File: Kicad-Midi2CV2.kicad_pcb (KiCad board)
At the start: 2 copper layers, 100 x 100 mm, 115 parts, among them IC101 MCP4725module, IC102 MCP4725module, J101 Doepfer connector, J102 Vin 7-12v, J103 MIDI OUT, J104 Power Conn, J105 CV7 in, J106 Gate1, J107 MIDI IN, J108 CV6 in, J109 Gate2, J110 CV3 in, J111 Gate3, J112 CV1, J113 Gate4, J114 CV2, J115 ControlConn, J116 ControlConn, J117 I2C_Conn, J118 I2C_Conn, Q101 MMBT2222A, Q102 MMBT2222A, SW101 Rotary_Encoder_Switch, U101 TL072, U102 TL072, U103 EL814

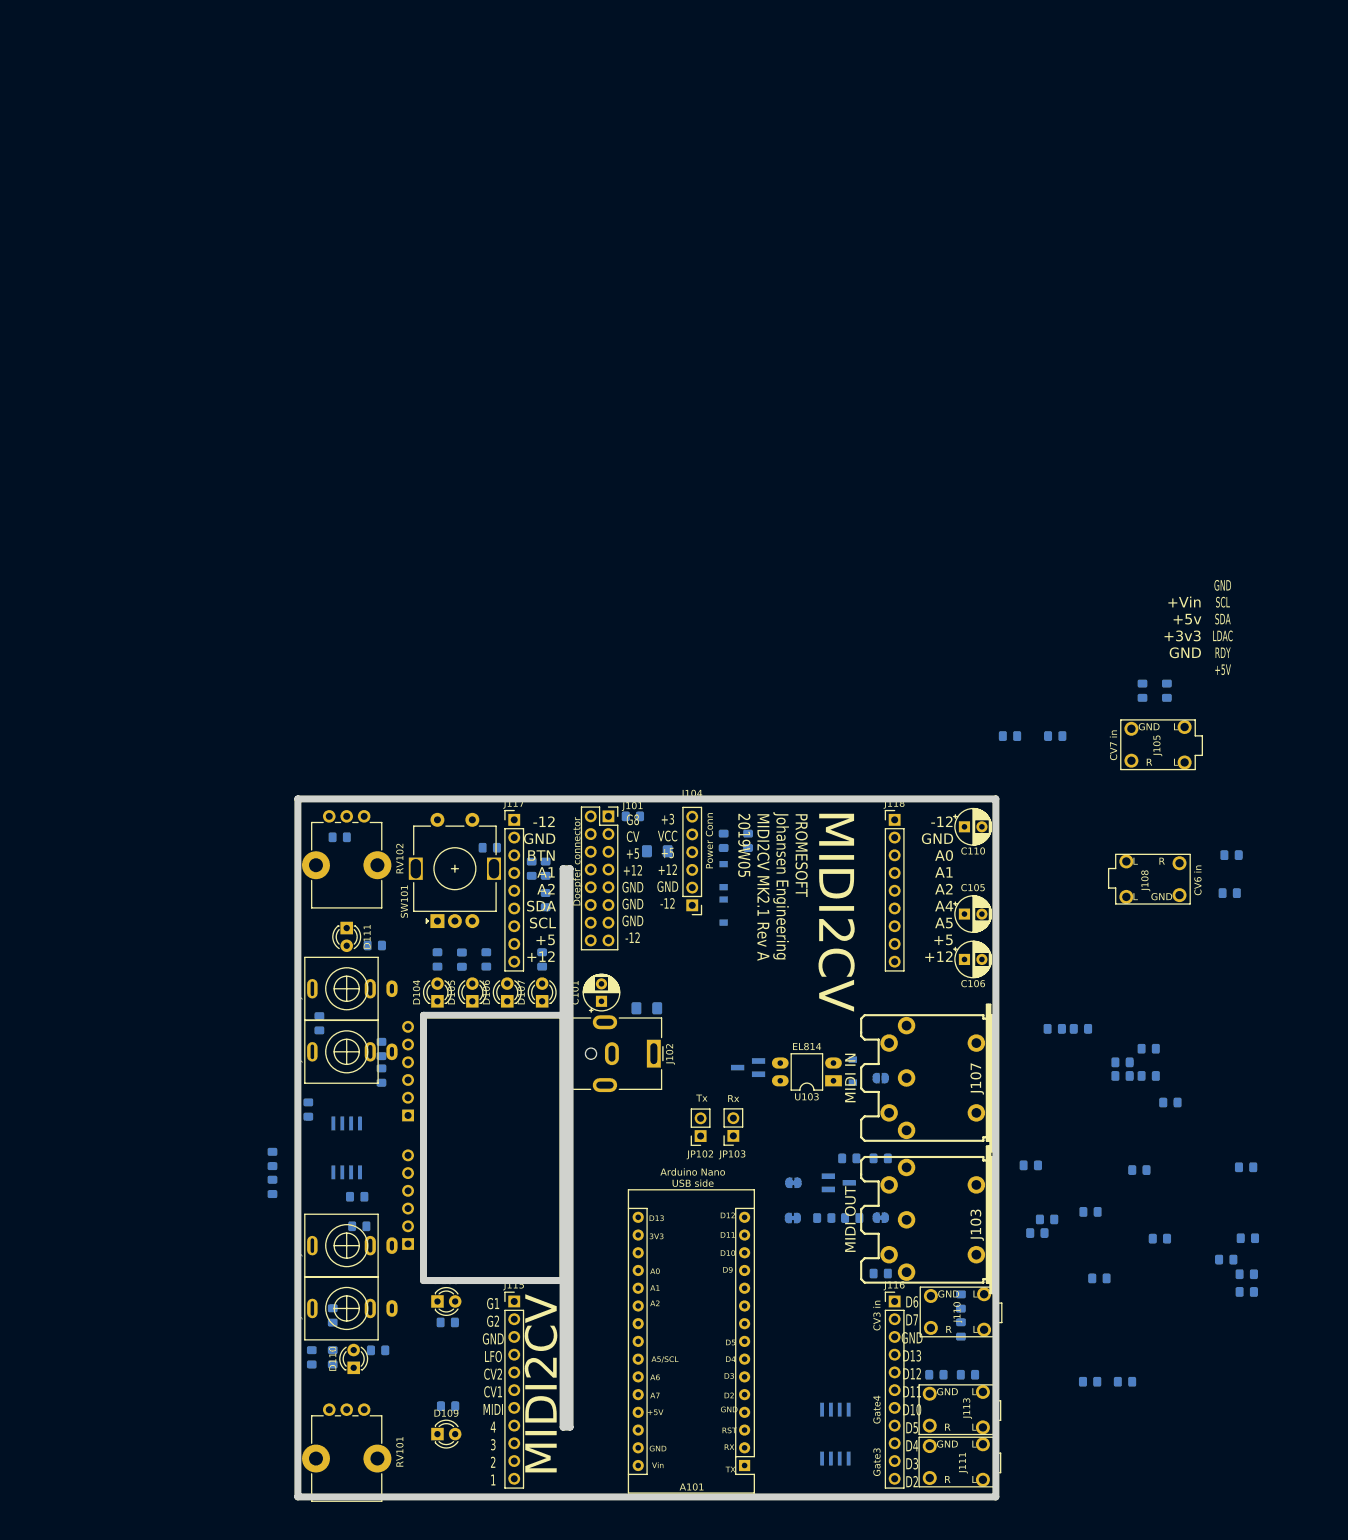
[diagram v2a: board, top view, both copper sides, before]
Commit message: Component replacement
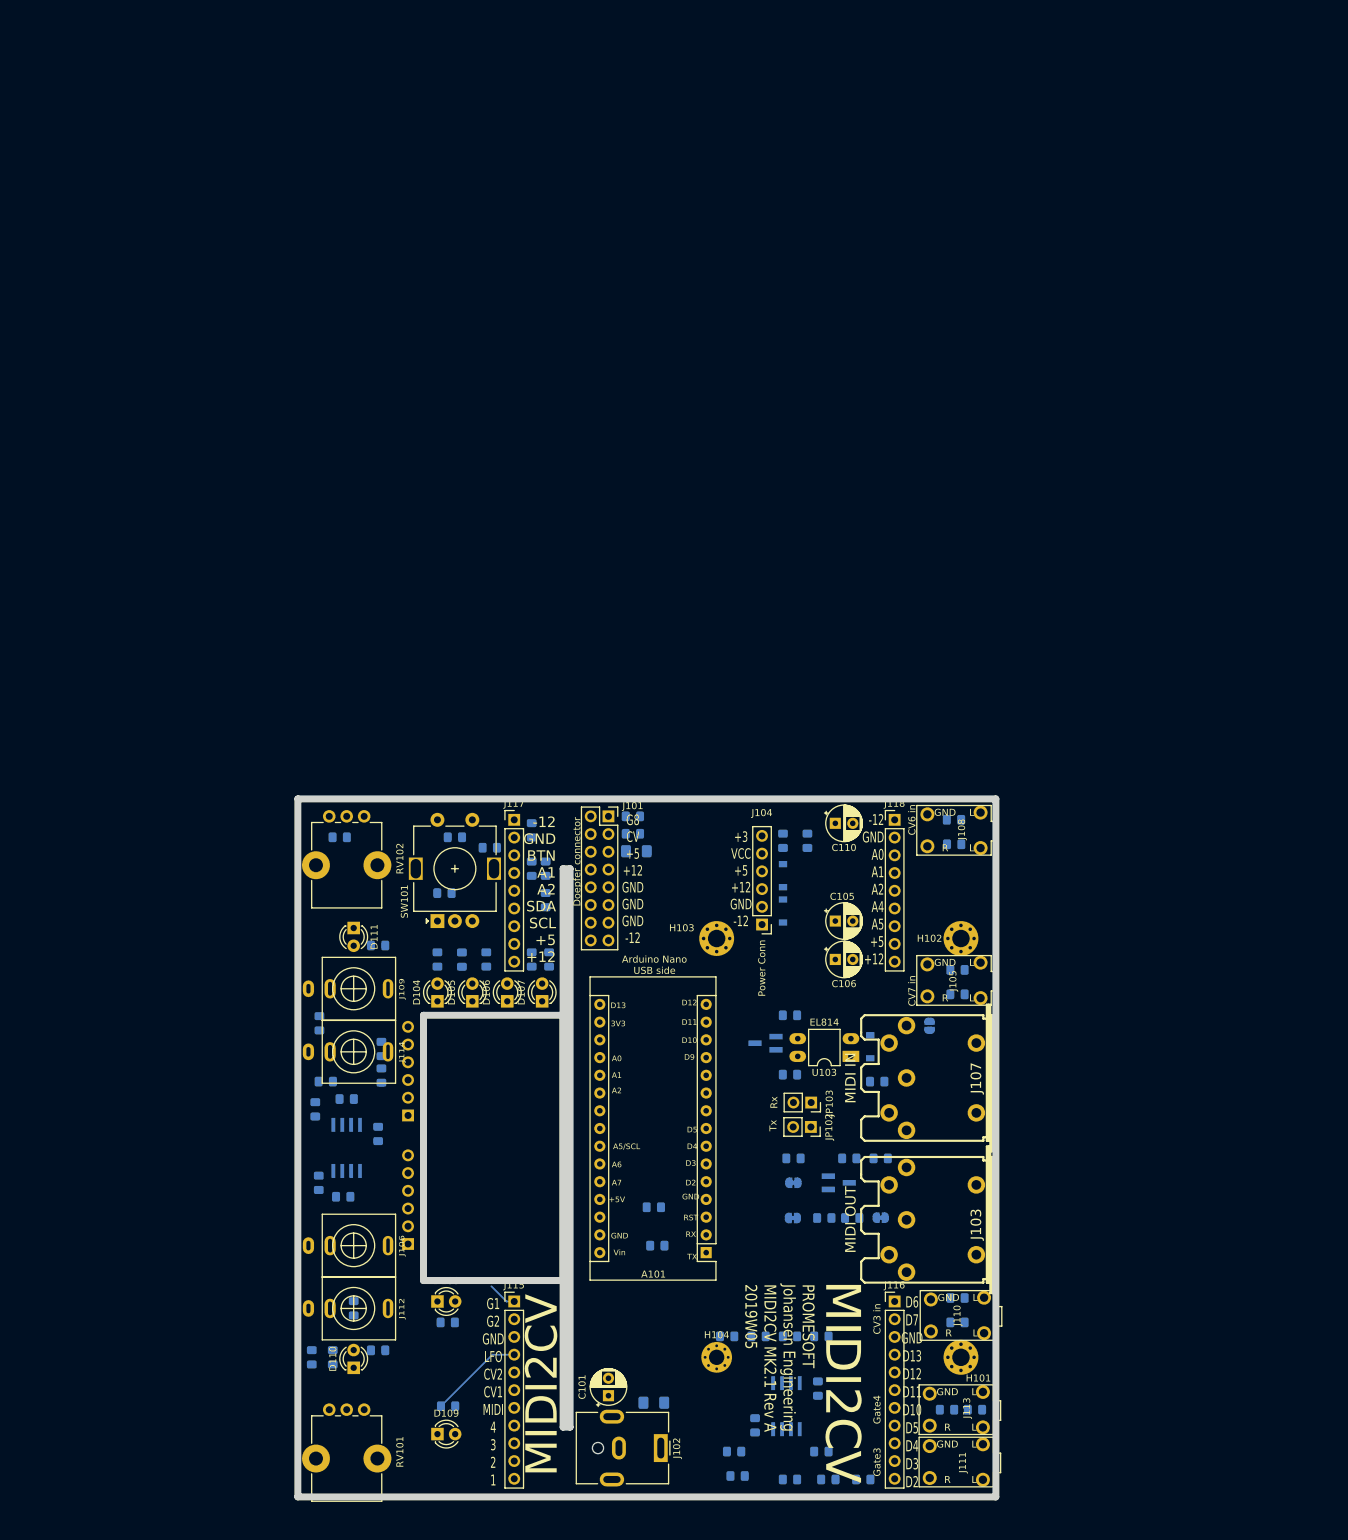
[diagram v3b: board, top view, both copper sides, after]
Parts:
- added H101: 2,5mm, MountingHole:MountingHole_2.5mm_Pad_Via, F.Cu at (195.0, 130.0)
- added H102: 2,5mm, MountingHole:MountingHole_2.5mm_Pad_Via, F.Cu at (195.0, 70.0)
- added H103: 2,2mm, MountingHole:MountingHole_2.5mm_Pad_Via, F.Cu at (160.0, 70.0)
- added H104: 2,2mm, MountingHole:MountingHole_2.2mm_M2_Pad_Via, F.Cu at (160.0, 130.0)
- C114: value 47n -> 11n
- C115: value 47n -> 22n
- C117, C118: value 100n -> 33n
- C119, C120: value 100n -> 44n
- R104, R105: value 10k -> 11k
- R108: value 100R -> 110R
- R113, R114: value 10k -> 22k
- R118: value 100R -> 220R
- R123, R124, R128, R129: value 10k -> 33k
- R135, R136, R138, R139: value 10k -> 44k
- moved C115 135.3 mm to (104.0, 90.5)
- moved R123 111.3 mm to (162.5, 143.5), turned to 180 degrees
- moved R144 103.3 mm to (121.0, 63.5)
- moved C121 100.9 mm to (122.5, 55.5)
- moved C116 84.5 mm to (151.5, 114.0)
- moved C109 81.5 mm to (133.5, 73.0), turned to 90 degrees
- moved R114 80.5 mm to (107.0, 93.0)
- moved R102 79.2 mm to (148.0, 55.0), turned to 180 degrees
- moved C118 78.5 mm to (163.0, 147.0)
- moved R127 73.2 mm to (194.0, 53.0)
- moved R138 71.8 mm to (161.5, 127.0)
- moved C117 70.0 mm to (170.5, 147.5)
- moved C113 69.8 mm to (133.5, 54.5), turned to 270 degrees
- moved C103 64.6 mm to (151.0, 108.5), turned to 180 degrees
- moved C119 64.1 mm to (166.0, 127.0)
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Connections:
- J106 pad S: Net-(J106-PadS) -> GND
- J109 pad S: Net-(J106-PadS) -> GND
- J111 pad S: Net-(J106-PadS) -> GND
- J113 pad S: Net-(J106-PadS) -> GND
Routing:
- net LED_LFO: track 0.00 -> 13.6 mm
- net Gate1: track 0.00 -> 4.18 mm
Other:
- board text removed: "+Vin +5v +3v3 GND"
- board text removed: "GND SCL SDA LDAC RDY +5V"

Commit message: Routing....
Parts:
- moved R141 10.0 mm to (121.5, 147.0)
- moved C115 7.63 mm to (110.5, 86.5), turned to 90 degrees
- moved C104 7.42 mm to (110.5, 82.5)
- moved R144 6.40 mm to (117.0, 68.5), turned to 90 degrees
- moved C121 5.70 mm to (128.0, 57.0), turned to 180 degrees
- moved R143 4.95 mm to (108.0, 74.5), turned to 90 degrees
- moved IC101 4.24 mm to (115.5, 118.0)
- moved R146 4.03 mm to (128.0, 53.0)
- moved C109 3.64 mm to (132.5, 76.5)
- moved R106 3.48 mm to (113.0, 82.5)
- moved R118 1.80 mm to (107.0, 57.0), turned to 90 degrees
- moved R107 1.09 mm to (113.0, 90.0)
- moved IC102 0.90 mm to (115.5, 94.5)
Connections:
- J115 pad 1: Gate1 -> LED4
- J115 pad 10: LED2 -> LED-CV1
- J115 pad 11: LED1 -> LED_LFO
- J115 pad 2: Gate2 -> LED3
- J115 pad 3: Net-(J115-Pad3) -> LED2
- J115 pad 4: LED_LFO -> LED1
- J115 pad 5: LED-CV2 -> Gate2
- J115 pad 6: LED-CV1 -> Gate1
- J115 pad 7: LED-MIDI -> GND
- J115 pad 8: LED4 -> LED-CV2
- J115 pad 9: LED3 -> LED-MIDI
- J116 pad 1: Gate1 -> LED4
- J116 pad 10: LED2 -> LED-CV1
- J116 pad 11: LED1 -> LED_LFO
- J116 pad 2: Gate2 -> LED3
- J116 pad 3: Net-(J115-Pad3) -> LED2
- J116 pad 4: LED_LFO -> LED1
- J116 pad 5: LED-CV2 -> Gate2
- J116 pad 6: LED-CV1 -> Gate1
- J116 pad 7: LED-MIDI -> GND
- J116 pad 8: LED4 -> LED-CV2
- J116 pad 9: LED3 -> LED-MIDI
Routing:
- net SDA: track 0.00 -> 64.0 mm
- net SCL: track 0.00 -> 61.8 mm
- net Net-(R118-Pad2): track 0.00 -> 52.2 mm
- net +5V: track 0.00 -> 47.9 mm, vias 0 -> 3
- net Net-(R108-Pad2): track 0.00 -> 45.7 mm
- net Net-(R114-Pad1): track 0.00 -> 42.7 mm, vias 0 -> 2
- net CV2Gain: track 0.00 -> 34.1 mm
- net GND: track 0.00 -> 32.5 mm
- net Net-(R104-Pad1): track 0.00 -> 28.0 mm
- net Gate1: track 4.18 -> 32.1 mm
- net LED-CV1: track 0.00 -> 27.7 mm
- net LED-MIDI: track 0.00 -> 23.3 mm
- net A1: track 0.00 -> 20.3 mm
- net CV1: track 0.00 -> 18.1 mm
- net A2: track 0.00 -> 14.9 mm
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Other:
- board text added: "4 3 2 1 G2 G1 GND CV2 MIDI CV1 LFO"
- board text added: "D5 D4 D3 D2 D7 D6 GND D12 D10 D11 D13"
- board text removed: "D6 D7 GND D13 D12 D11 D10 D5 D4 D3 D2"
- board text removed: "G1 G2 GND LFO CV2 CV1 MIDI 4 3 2 1"

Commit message: front routed....
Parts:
- moved C114 0.50 mm to (108.5, 123.0)
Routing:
- net LED2: track 0.00 -> 138.5 mm, vias 0 -> 4
- net LED1: track 0.00 -> 138.4 mm, vias 0 -> 9
- net LED4: track 0.00 -> 104.4 mm, vias 0 -> 7
- net LED3: track 0.00 -> 95.0 mm, vias 0 -> 7
- net Gate2: track 0.00 -> 73.4 mm, vias 0 -> 6
- net -12V: track 5.41 -> 77.8 mm, vias 0 -> 4
- net +12V: track 5.15 -> 73.9 mm, vias 0 -> 8
- net +5V: track 47.9 -> 71.7 mm, vias 3 -> 4
- net GND: track 32.5 -> 54.0 mm, vias 0 -> 4
- net CV1Gain: track 8.27 -> 13.1 mm, vias 0 -> 1
- net CV2Gain: track 34.1 -> 36.1 mm
- net Gate1: track 32.1 -> 33.5 mm
- net CV1: track 18.1 -> 18.9 mm
- net Net-(R118-Pad2): track 52.2 -> 52.8 mm

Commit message: Initial PCB finished - no DRC
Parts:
- added R147: 133R, Resistor_SMD:R_0805_2012Metric_Pad1.15x1.40mm_HandSolder, B.Cu at (177.0, 141.0)
- added R148: 144R, Resistor_SMD:R_0805_2012Metric_Pad1.15x1.40mm_HandSolder, B.Cu at (173.0, 128.0)
- JP104: value GND MIDI OUT -> GND MIDI IN
- moved C116 36.9 mm to (175.0, 85.5), turned to 270 degrees
- moved R135 26.6 mm to (169.0, 126.0)
- moved R136 26.6 mm to (173.0, 126.0)
- moved R128 12.3 mm to (169.0, 145.0), turned to 180 degrees
- moved R111 9.53 mm to (179.0, 105.0)
- moved C119 7.62 mm to (173.0, 124.0), turned to 180 degrees
- moved C118 7.21 mm to (169.0, 143.0), turned to 180 degrees
- moved C105 7.00 mm to (177.0, 60.5)
- moved R123 6.96 mm to (169.0, 141.0)
- moved C120 6.71 mm to (169.0, 124.0), turned to 180 degrees
- moved R139 6.18 mm to (169.0, 121.0)
- moved C117 5.15 mm to (173.0, 143.0)
- moved R115 5.00 mm to (171.0, 110.0), turned to 0 degrees
- moved C103 4.61 mm to (146.5, 107.5)
- moved R138 4.61 mm to (165.0, 124.0), turned to 180 degrees
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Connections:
- U102 pad 1: Gate3Gain -> Net-(R147-Pad2)
- U102 pad 7: Gate4Gain -> Net-(R148-Pad2)
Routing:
- net +5V: track 71.7 -> 251.3 mm, vias 4 -> 6
- net LED-CV2: track 0.00 -> 176.5 mm, vias 0 -> 6
- net -12V: track 77.8 -> 245.5 mm, vias 4 -> 12
- net +12V: track 73.9 -> 217.2 mm, vias 8 -> 15
- net GND: track 54.0 -> 194.2 mm, vias 4 -> 14
- net A7: track 0.00 -> 131.8 mm, vias 0 -> 1
- net A3: track 0.00 -> 115.0 mm, vias 0 -> 5
- net A6: track 0.00 -> 113.3 mm, vias 0 -> 1
- net LED_LFO: track 12.1 -> 121.7 mm
- net VCC: track 0.00 -> 103.4 mm, vias 0 -> 3
- net LED-CV1: track 27.7 -> 119.4 mm
- net LED-MIDI: track 23.3 -> 104.9 mm
- net Gate3: track 0.00 -> 62.2 mm, vias 0 -> 2
- net SCL: track 61.8 -> 123.5 mm
- net Gate1: track 33.5 -> 93.0 mm
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- added copper zone on F.Cu, net GND

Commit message: GND plane
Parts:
- moved R137 0.60 mm to (135.4, 73.0)
- moved C114 0.50 mm to (109.0, 123.0)
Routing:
- net A3: track 115.0 -> 125.5 mm
- net +12V: track 217.2 -> 224.6 mm
- net GND: track 194.2 -> 200.8 mm, vias 14 -> 15
- net LED-CV2: track 176.5 -> 182.1 mm, vias 6 -> 8
- net LED2: track 175.8 -> 179.9 mm, vias 4 -> 10
- net CV1Gain: track 13.1 -> 16.9 mm
- net Net-(R114-Pad1): track 42.7 -> 46.3 mm
- net -12V: track 245.5 -> 247.5 mm, vias 12 -> 10
- net Net-(J105-PadT): track 11.5 -> 10.0 mm
- net Net-(R104-Pad1): track 28.2 -> 29.6 mm
- net Gate4Gain: track 42.1 -> 43.3 mm
- net LED1: track 175.7 -> 176.8 mm, vias 9 -> 11
- net Gate3Gain: track 36.6 -> 35.6 mm
- net /Q1Emitter: track 20.4 -> 20.9 mm
- net Gate2: track 128.8 -> 128.3 mm
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
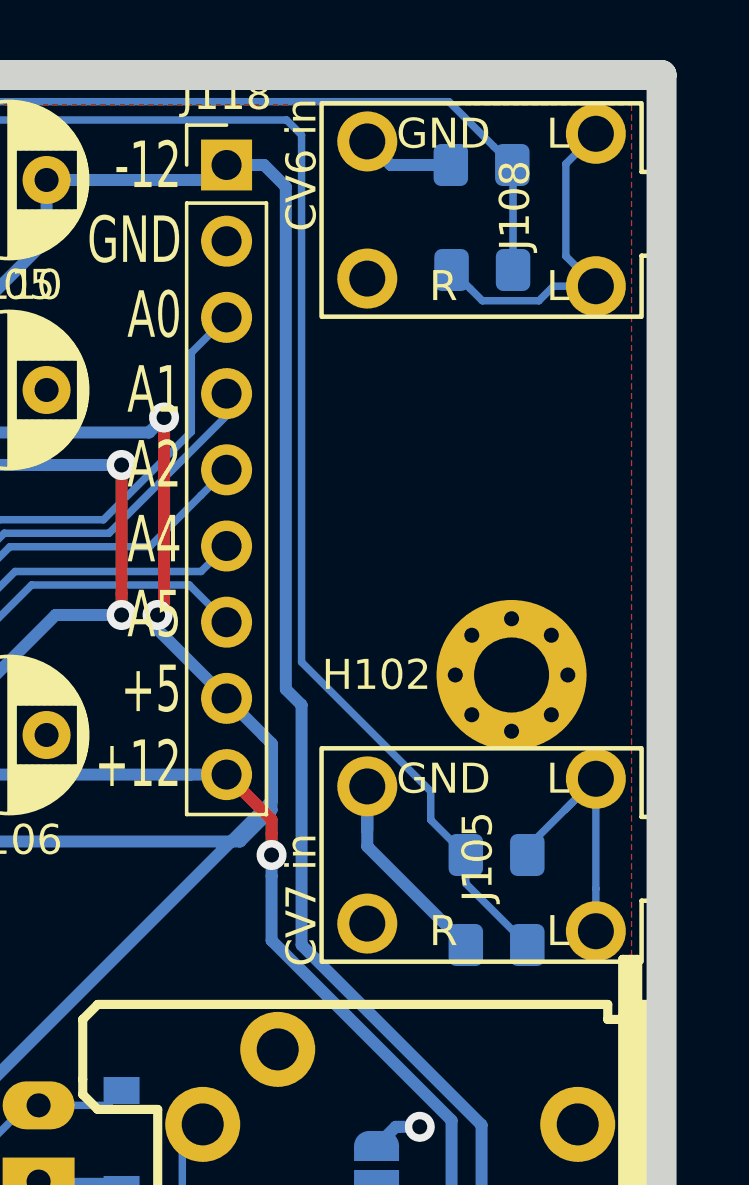
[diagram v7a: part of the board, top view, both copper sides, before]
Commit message: Component text on PCB
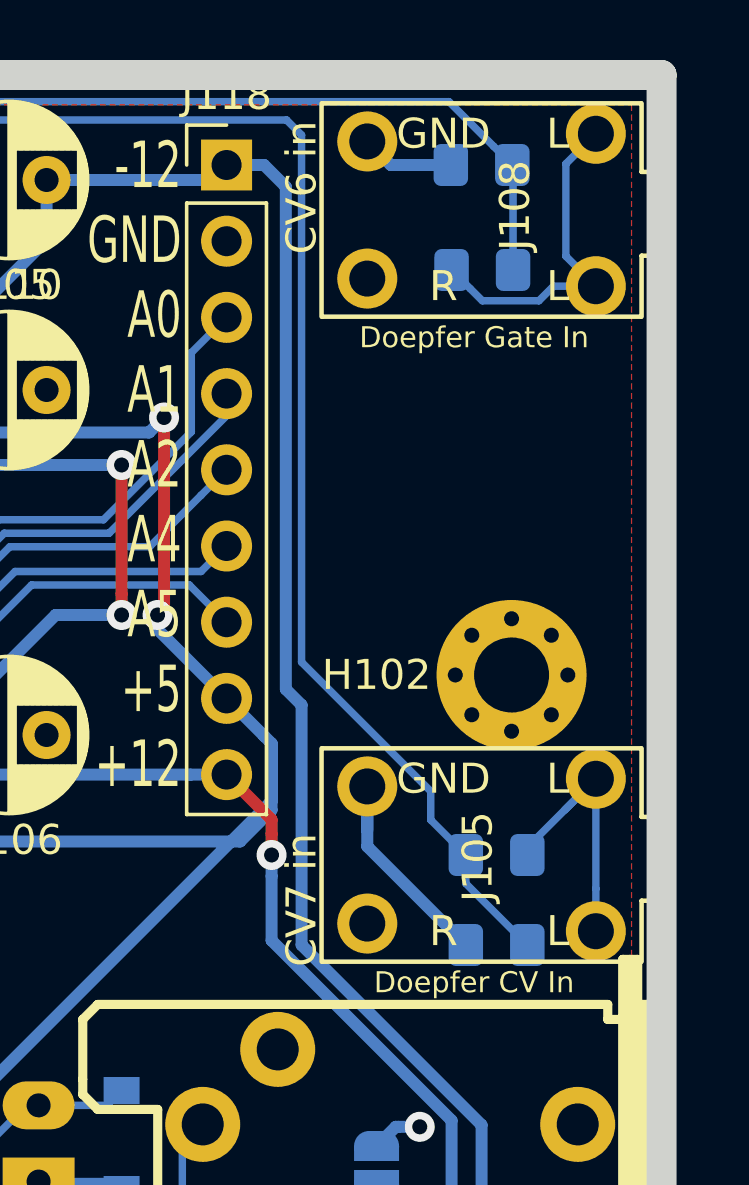
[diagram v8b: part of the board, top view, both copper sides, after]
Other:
- board text added: "Doepfer CV In"
- board text added: "Doepfer Gate In"
